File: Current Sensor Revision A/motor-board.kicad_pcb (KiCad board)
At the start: 2 copper layers, 98 x 48 mm, 26 parts, among them J1 SMA, J3 Screw_Terminal_01x02, U1 ACS37030, U2 MCP633

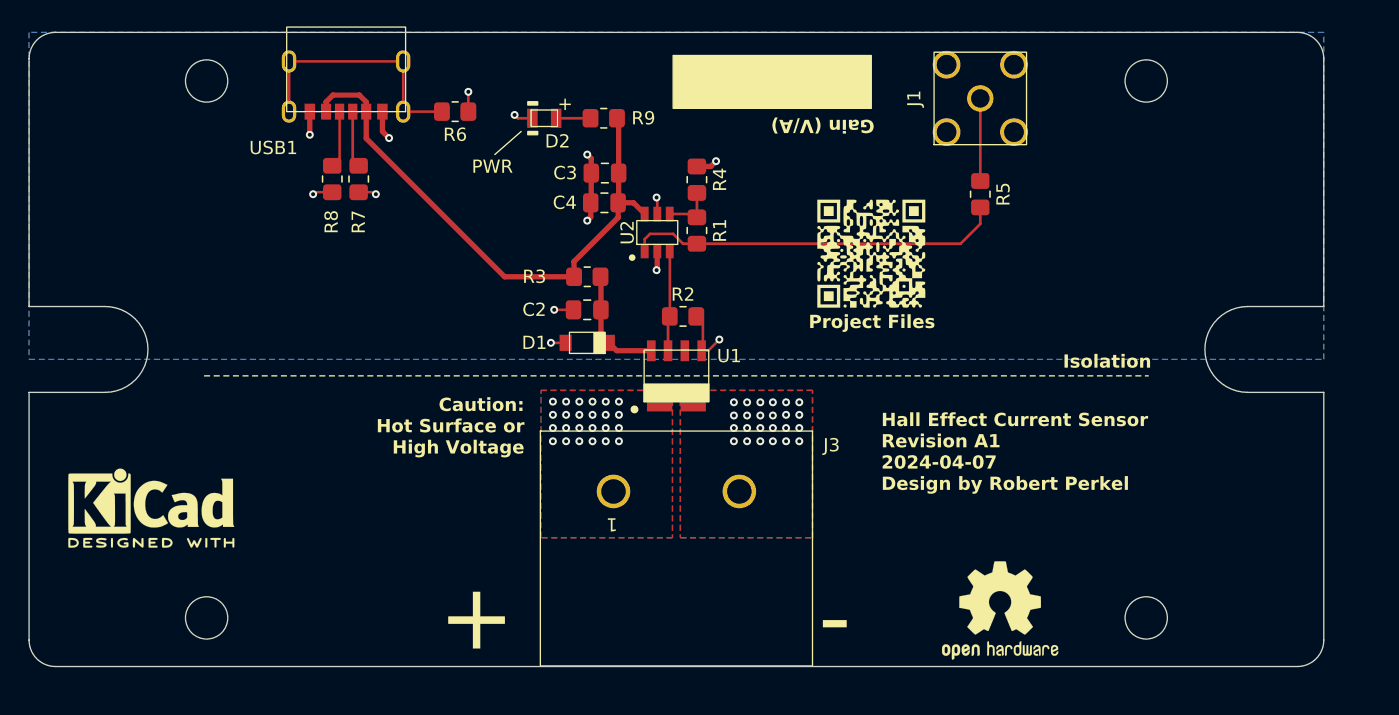
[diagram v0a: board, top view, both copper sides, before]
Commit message: Added A2/A3 PCB files and 3D Board Render
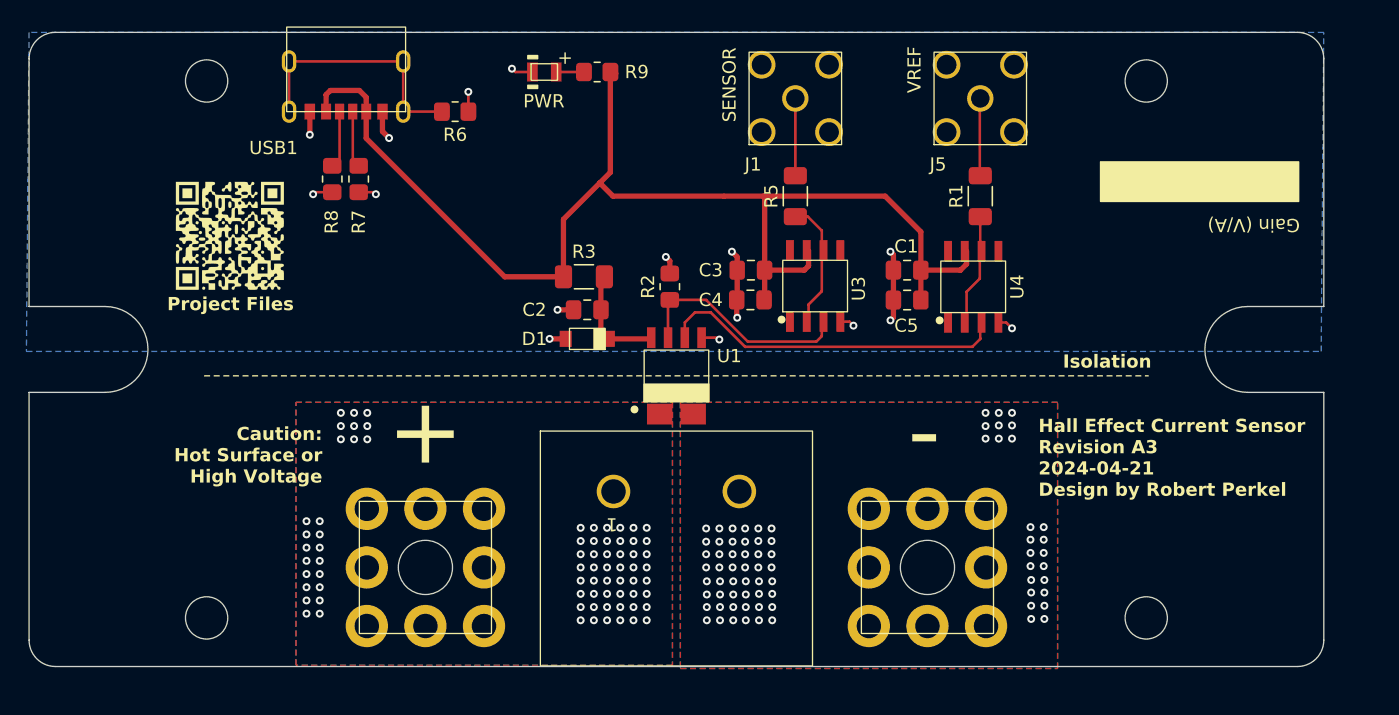
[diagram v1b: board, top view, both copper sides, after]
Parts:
- removed R4: 1.8k, Resistor_SMD:R_0805_2012Metric_Pad1.20x1.40mm_HandSolder
- removed the REF** at (171.5, 135.8)
- removed the REF** at (107.2, 128.0)
- removed U2: MCP633, StandardPackages_Custom:SOT23-6
- added C1: 0.1uF, Capacitor_SMD:C_0805_2012Metric_Pad1.18x1.45mm_HandSolder, F.Cu at (164.5, 110.0)
- added C5: 10uF, Capacitor_SMD:C_0805_2012Metric_Pad1.18x1.45mm_HandSolder, F.Cu at (164.5, 112.3)
- added J2: 74650094R, Current Sensor PCB Library:74650094R, F.Cu at (128.0, 132.5)
- added J4: 74650094R, Current Sensor PCB Library:74650094R, F.Cu at (166.0, 132.5)
- added J5: SMA, Current Sensor PCB Library:CONSMA002-L-G, F.Cu at (170.0, 97.0)
- added U3: MCP631, StandardPackages_Custom:SOIC-8, F.Cu at (157.5, 111.2)
- added U4: MCP631, StandardPackages_Custom:SOIC-8, F.Cu at (169.5, 111.3)
- R1: value 910 -> 50; footprint Resistor_SMD:R_0805_2012Metric_Pad1.20x1.40mm_HandSolder -> Resistor_SMD:R_1206_3216Metric_Pad1.30x1.75mm_HandSolder
- R3, R5: footprint Resistor_SMD:R_0805_2012Metric_Pad1.20x1.40mm_HandSolder -> Resistor_SMD:R_1206_3216Metric_Pad1.30x1.75mm_HandSolder
- moved G*** 48.6 mm to (113.2, 107.4)
- moved R1 21.6 mm to (170.0, 104.4), turned to 90 degrees
- moved R5 14.0 mm to (156.0, 104.4)
- moved J1 14.0 mm to (156.0, 97.0)
- moved C3 13.3 mm to (152.6, 110.0)
- moved C4 13.3 mm to (152.6, 112.2)
- moved R9 3.54 mm to (141.0, 95.0)
- moved D2 3.50 mm to (137.0, 95.0)
- moved R2 2.46 mm to (146.5, 111.2), turned to 90 degrees
- moved D1 0.30 mm to (140.2, 115.2)
- moved R3 0.25 mm to (140.0, 110.5)
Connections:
- R1 pad 2: Net-(U2-VOUT) -> Net-(J5-In)
- R5 pad 1: Net-(U2-VOUT) -> Net-(U3-IN-)
- U1 pad 4: unconnected-(U1-VREF/FAULT-Pad4) -> VREF
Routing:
- net +5V: track 42.8 -> 92.3 mm
- net Net-(U2-VOUT): track 28.6 -> 0.00 mm
- net VREF: track 0.00 -> 26.4 mm
- net Net-(U3-IN-): track 0.00 -> 9.75 mm
- net /SENSOR_OUT: track 7.60 -> 17.0 mm
- net Net-(J5-In): track 0.00 -> 5.98 mm
- net Net-(U4-IN-): track 4.22 -> 8.35 mm
- net GND: track 26.8 -> 28.2 mm, vias 14 -> 16
- net Net-(D1-K): track 8.72 -> 8.17 mm
- net /IP-: vias 24 -> 73
- net /IP+: vias 24 -> 73
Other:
- board text added: "SENSOR"
- board text added: "VREF"
